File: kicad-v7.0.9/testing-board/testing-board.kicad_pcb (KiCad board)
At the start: 2 copper layers, 31.1 x 73 mm, 39 parts, among them J1 54601-908WPLF, J2 EBBA-02-C-SS-BU, P1 DS1021-1-3SF11-B, P10 10129380-902001BLF, P11 10129380-902001BLF, P12 10129380-902001BLF, P13 10129380-902001BLF, P14 10129380-902001BLF, P2 DS1023-1-3S21, P3 DS1021-1-4SF11-B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

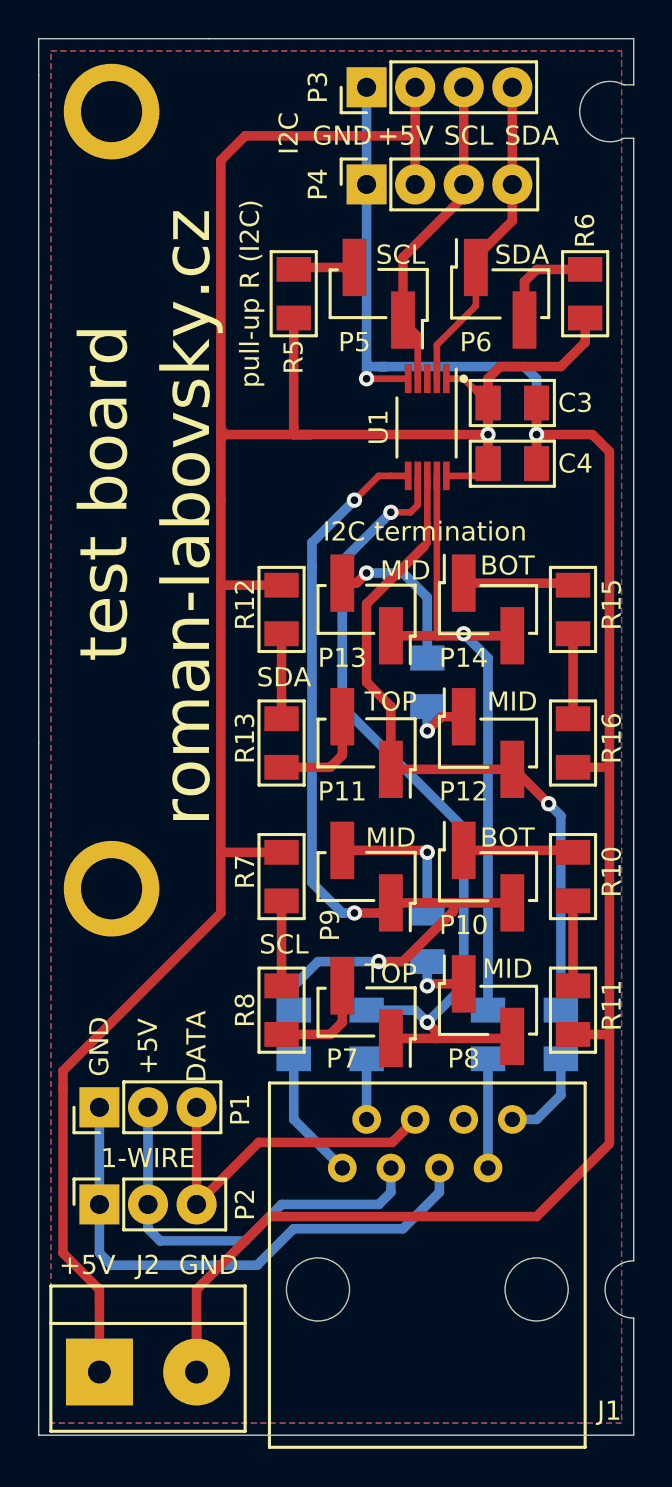
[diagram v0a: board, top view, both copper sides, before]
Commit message: Change of components from edited library. Change folder structure.
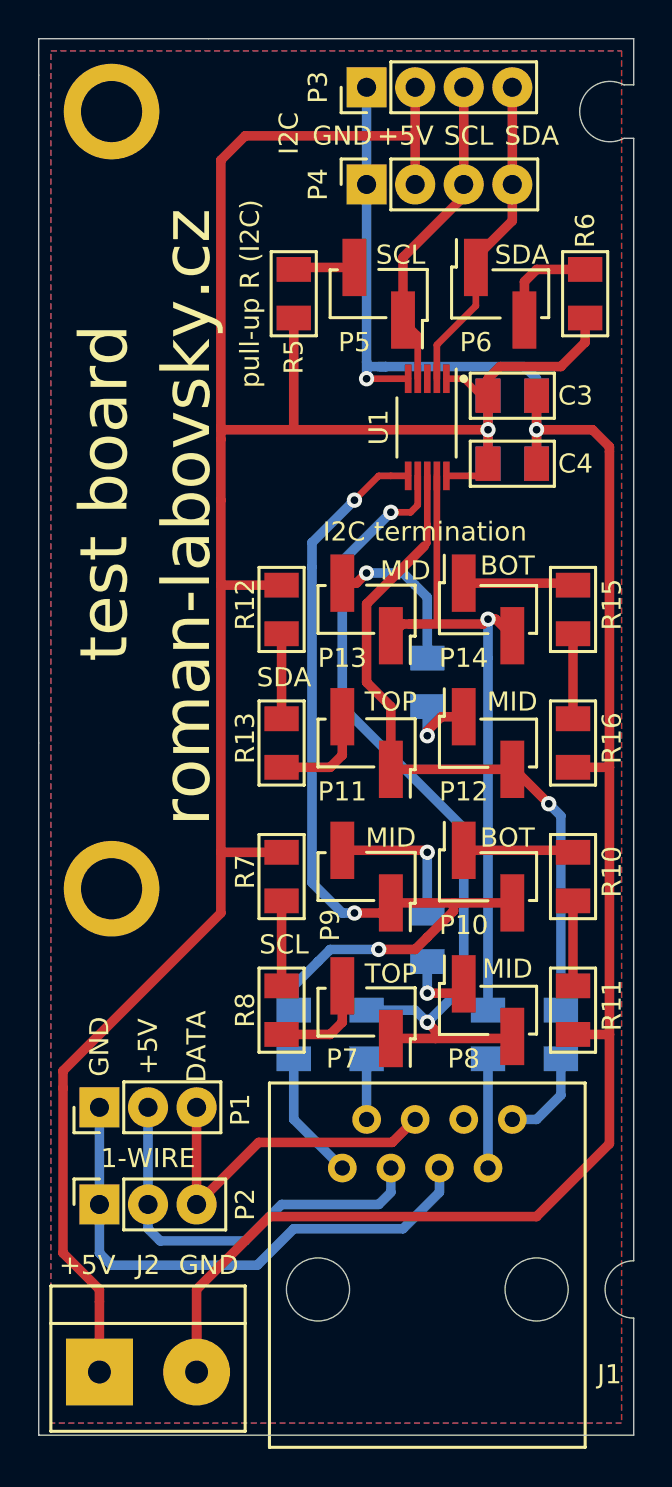
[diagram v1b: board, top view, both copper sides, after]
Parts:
- J1: footprint connector_rl:rj45_54601-908WPLF -> connector_rj45_tht_rl:54601-908WPLF
- moved C1 0.38 mm to (139.7, 80.3)
- moved C3 0.38 mm to (139.7, 80.3)
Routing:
- net /DSDA_N: track 34.9 -> 37.1 mm
- net +5V: track 129.5 -> 128.2 mm
- net Net-(P8-Pad1): track 3.22 -> 3.76 mm
- net Net-(P12-Pad1): track 3.48 -> 3.99 mm

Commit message: Change components form library. Adding of BOM.
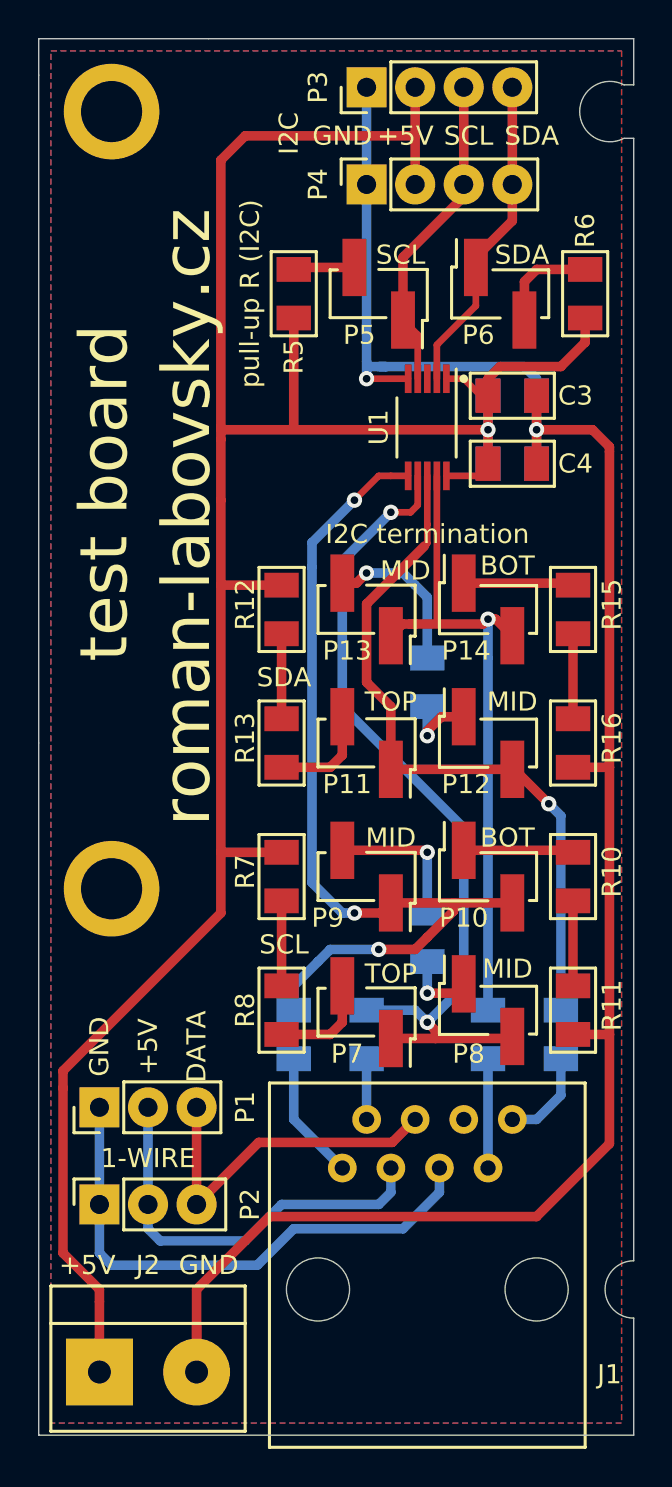
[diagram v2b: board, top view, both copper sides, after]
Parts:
- P1: footprint connector_tht_pinheader_2.54mm_rl:1x3_pinheader_2.54mm_vertical -> connector_pin_header_2.54mm_tht_rl:1x3_pin_header_2.54mm_vertical
- P10, P11, P12, P13, P14, P5, P6, P7, P8, P9: footprint connector_smd_pinheader_2.54mm_rl:1x2_pinheader_2.54mm_vertical -> connector_pin_header_2.54mm_smd_rl:1x2_pin_header_2.54mm_vertical
- P2: footprint connector_tht_pinsocket_2.54mm_rl:1x3_pinsocket_2.54mm_vertical_8.4mm -> connector_pin_socket_2.54mm_tht_rl:1x3_pin_socket_2.54mm_vertical_8.5mm
- P3: footprint connector_tht_pinheader_2.54mm_rl:1x4_pinheader_2.54mm_vertical -> connector_pin_header_2.54mm_tht_rl:1x4_pin_header_2.54mm_vertical
- P4: footprint connector_tht_pinsocket_2.54mm_rl:1x4_pinsocket_2.54mm_vertical_8.4mm -> connector_pin_socket_2.54mm_tht_rl:1x4_pin_socket_2.54mm_vertical_8.5mm
